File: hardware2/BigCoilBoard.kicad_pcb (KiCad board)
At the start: 2 copper layers, 124 x 76.5 mm, 138 parts, among them J1 Conn_01x02, J10 PFC_OUT, J11 THERM2_IN, J12 THERM3_IN, J13 THERM4_IN, J14 THERM5_IN, J15 Conn_01x03, J16 Conn_ARM_JTAG_SWD_10, J17 Conn_01x04, J18 Conn_01x04, J19 Conn_01x04, J2 Conn_01x02, J20 Screw_Terminal_01x01, J21 Screw_Terminal_01x01, J22 Screw_Terminal_01x01, J23 Screw_Terminal_01x01, J3 Conn_01x03_Pin, J5 THERM1_IN, J6 Conn_01x03_Pin, J7 Conn_01x04, J8 CONTACTOR_1, J9 CONTACTOR_2, K1 G5NB-1A-DC24, K2 G5NB-1A-DC24, Q1 T2N7002AK, Q2 T2N7002AK, Q3 T2N7002AK, Q4 T2N7002AK, Q5 T2N7002AK, Q6 T2N7002AK, Q7 T2N7002AK, U1 STM32G474CBTx, U10 IF-D95, U11 IF-E96E, U12 LD1117S33TR_SOT223, U13 TC7662Bx0A, U14 L7812, U2 MCP6477-E/SN, U3 CSTNE8M00G550000R0, U4 MCP3208, U6 MGJ2D241709SC, U7 STGAP2SM, U8 SN74LV1T34DBV, U9 IF-D95

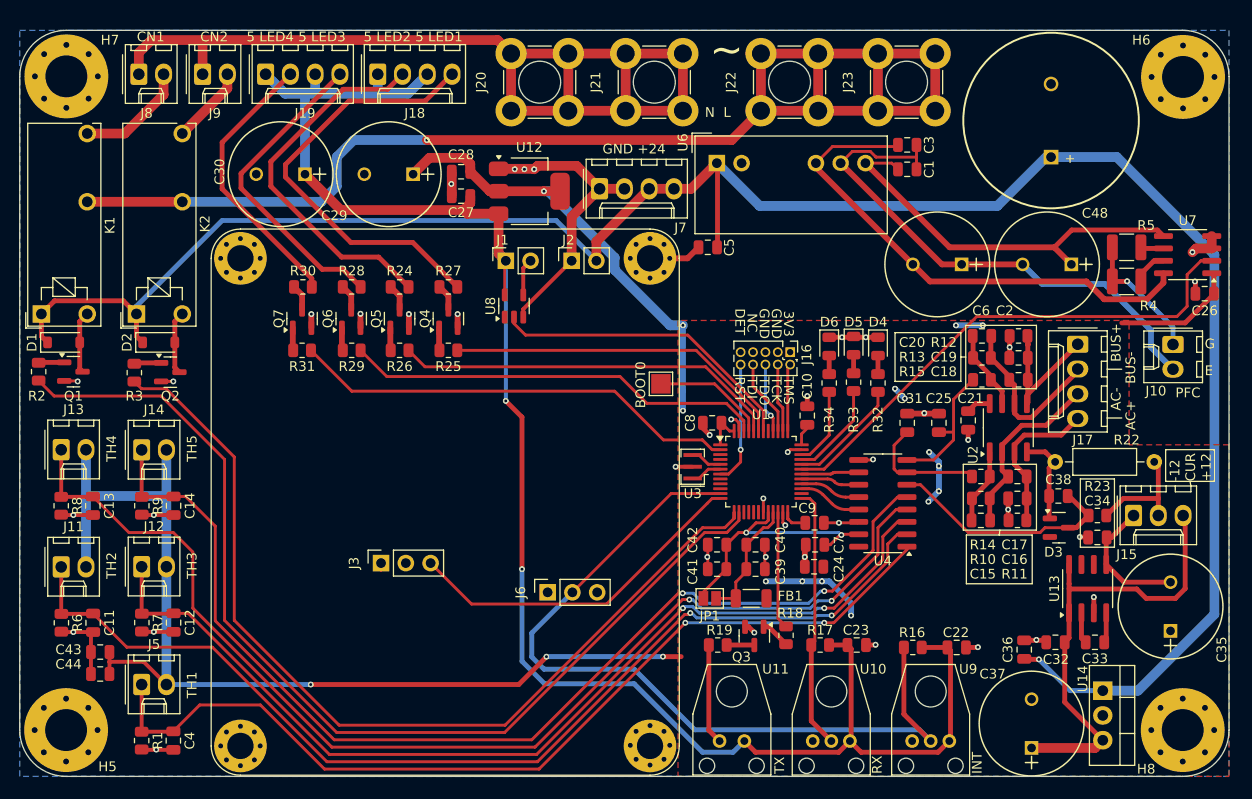
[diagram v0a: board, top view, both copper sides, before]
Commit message: back to int adc
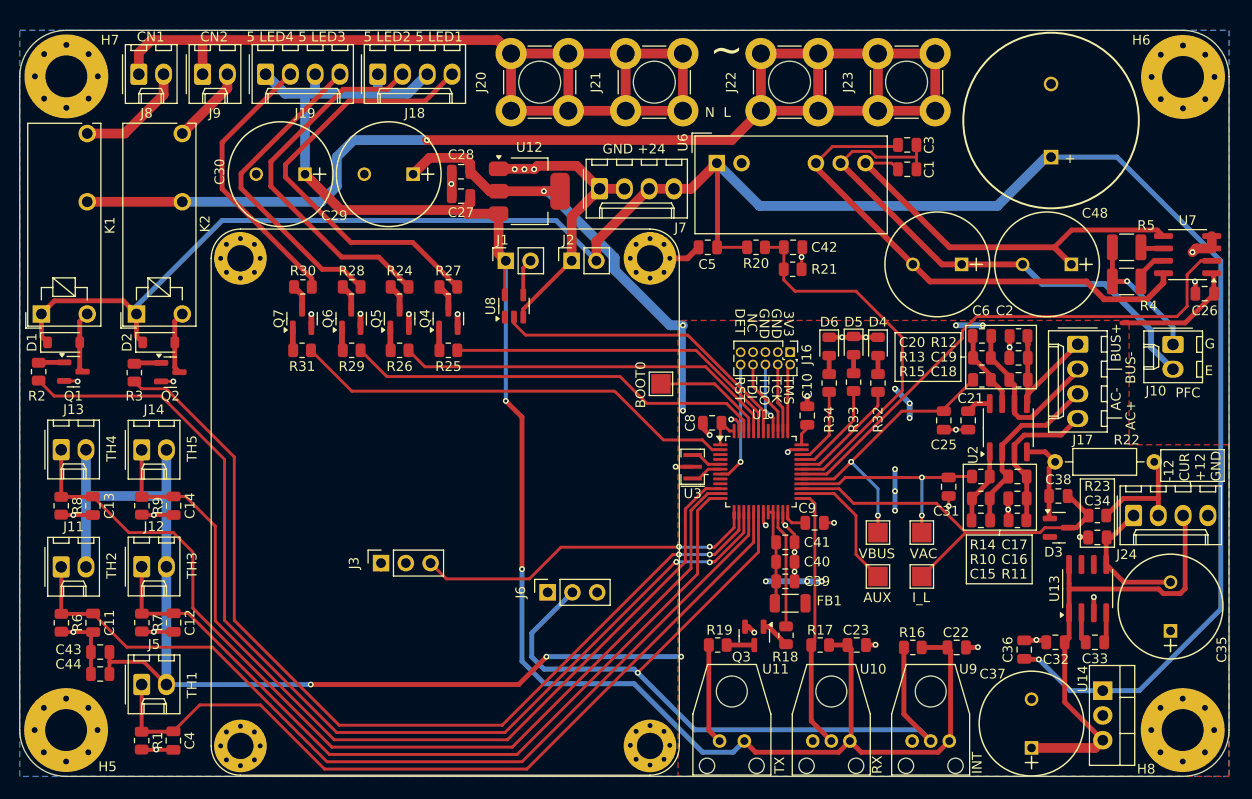
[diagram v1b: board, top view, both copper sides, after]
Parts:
- removed C24, C7: 0.1u, Capacitor_SMD:C_0805_2012Metric
- removed J15: Conn_01x03, Connector_Molex:Molex_KK-254_AE-6410-03A_1x03_P2.54mm_Vertical
- removed JP1: SolderJumper_2_Open, Jumper:SolderJumper-2_P1.3mm_Open_Pad1.0x1.5mm
- removed U4: MCP3208, Package_SO:SOIC-16_3.9x9.9mm_P1.27mm
- added J24: Conn_01x04, Connector_Molex:Molex_KK-254_AE-6410-04A_1x04_P2.54mm_Vertical, F.Cu at (220.5, 96.0)
- added R20: 10k, Resistor_SMD:R_0805_2012Metric, F.Cu at (181.8, 68.5)
- added R21: 1k, Resistor_SMD:R_0805_2012Metric, F.Cu at (185.5, 70.8)
- added TP3: TestPoint, TestPoint:TestPoint_Pad_2.0x2.0mm, F.Cu at (198.8, 102.2)
- added TP4: TestPoint, TestPoint:TestPoint_Pad_2.0x2.0mm, F.Cu at (198.8, 97.8)
- added TP5: TestPoint, TestPoint:TestPoint_Pad_2.0x2.0mm, F.Cu at (194.2, 97.8)
- added TP6: TestPoint, TestPoint:TestPoint_Pad_2.0x2.0mm, F.Cu at (194.2, 102.2)
- C41: value 0.1u -> 10n
- C42: value 10u -> 0.1u
- moved C42 31.5 mm to (185.6, 68.5), turned to 0 degrees
- moved C31 7.81 mm to (201.5, 93.0), turned to -90 degrees
- moved C41 7.52 mm to (184.8, 98.8), turned to 0 degrees
- moved FB1 4.03 mm to (185.2, 105.0)
- moved C40 3.52 mm to (184.8, 100.8)
- moved C39 3.30 mm to (184.8, 102.8)
- moved C25 0.56 mm to (201.0, 86.2), turned to -90 degrees
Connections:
- C41 pad 1: VREF -> +3.3VA
- C42 pad 1: VREF -> V24_SENSE
- U1 pad 10: unconnected-(U1-PA2-Pad10) -> THERM5
- U1 pad 11: INT_IN -> THERM4
- U1 pad 12: OCD_SET -> THERM3
- U1 pad 13: CN2 -> OCD_SET
- U1 pad 14: CN1 -> CN2
- U1 pad 15: unconnected-(U1-PA7-Pad15) -> CN1
- U1 pad 16: unconnected-(U1-PB0-Pad16) -> THERM2
- U1 pad 17: unconnected-(U1-PB1-Pad17) -> THERM1
- U1 pad 18: unconnected-(U1-PB2-Pad18) -> INT_IN
- U1 pad 20: VREF -> +3.3VA
- U1 pad 26: unconnected-(U1-PB12-Pad26) -> AUX_PIN
- U1 pad 27: SCK -> I_L
- U1 pad 28: MISO -> VAC_SENSE
- U1 pad 29: MOSI -> VBUS_SENSE
- U1 pad 30: CS -> PFC
- U1 pad 31: PFC -> V24_SENSE
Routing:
- net V24_SENSE: track 0.00 -> 39.0 mm
- net VREF: track 26.5 -> 0.00 mm, vias 2 -> 0
- net THERM5: track 112.2 -> 94.0 mm, vias 2 -> 0
- net THERM4: track 118.0 -> 100.7 mm, vias 2 -> 0
- net I_L: track 24.3 -> 41.3 mm
- net THERM3: track 101.1 -> 84.8 mm, vias 2 -> 0
- net VBUS_SENSE: track 14.6 -> 30.7 mm, vias 0 -> 2
- net THERM2: track 109.0 -> 93.6 mm, vias 2 -> 0
- net AUX_PIN: track 0.00 -> 13.7 mm
- net THERM1: track 96.8 -> 84.2 mm, vias 2 -> 0
- net VAC_SENSE: track 12.6 -> 22.9 mm, vias 0 -> 2
- net SCK: track 6.55 -> 0.00 mm
- net MISO: track 6.24 -> 0.00 mm
- net MOSI: track 6.01 -> 0.00 mm
- net CS: track 5.91 -> 0.00 mm
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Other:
- board text added: "-12 CUR +12 GND"
- board text added: "AUX"
- board text added: "I_L"
- board text added: "VAC"
- board text added: "VBUS"
- board text removed: "-12 CUR +12"
